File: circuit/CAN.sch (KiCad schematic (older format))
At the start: 4 parts

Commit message: 変更点忘れた
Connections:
- net +5V: no longer U?.3 (VDD)
- net TxD: now reaches U?.1 (TXD)
- net RxD: now reaches U?.4 (RXD)
- new net +3V3: U?.3 (VDD)
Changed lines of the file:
@@
 LIBS:robocon_sch
 LIBS:YASU
+LIBS:stm32
 LIBS:ServoDriver-cache
 EELAYER 25 0
@@
 $EndComp
 Wire Wire Line
-	3300 1900 3200 1900
+	3200 1900 3300 1900
 Wire Wire Line
 	3400 1900 3500 1900
@@
 	4600 1900 4700 1900
 Wire Wire Line
-	3700 1900 3600 1900
+	3600 1900 3700 1900
 Wire Wire Line
 	3650 1900 3650 2000
@@
 	1    0    0    -1
 $EndComp
-$Comp
-L +5V #PWR?
-U 1 1 594C7987
+Wire Wire Line
+	2250 1850 2250 1950
+$Comp
+L +3.3V #PWR?
+U 1 1 594E28CB
 P 2250 1850
 F 0 "#PWR?" H 2250 1700 50  0001 C CNN
-F 1 "+5V" H 2250 1990 50  0000 C CNN
+F 1 "+3.3V" H 2250 1990 50  0000 C CNN
 F 2 "" H 2250 1850 50  0001 C CNN
 F 3 "" H 2250 1850 50  0001 C CNN
@@
 $EndComp
 Wire Wire Line
-	2250 1850 2250 1950
+	1750 2250 1650 2250
+Wire Wire Line
+	1650 2150 1750 2150
+Text HLabel 1650 2250 0    60   Input ~ 0
+RxD
+Text HLabel 1650 2150 0    60   Output ~ 0
+TxD
 $EndSCHEMATC

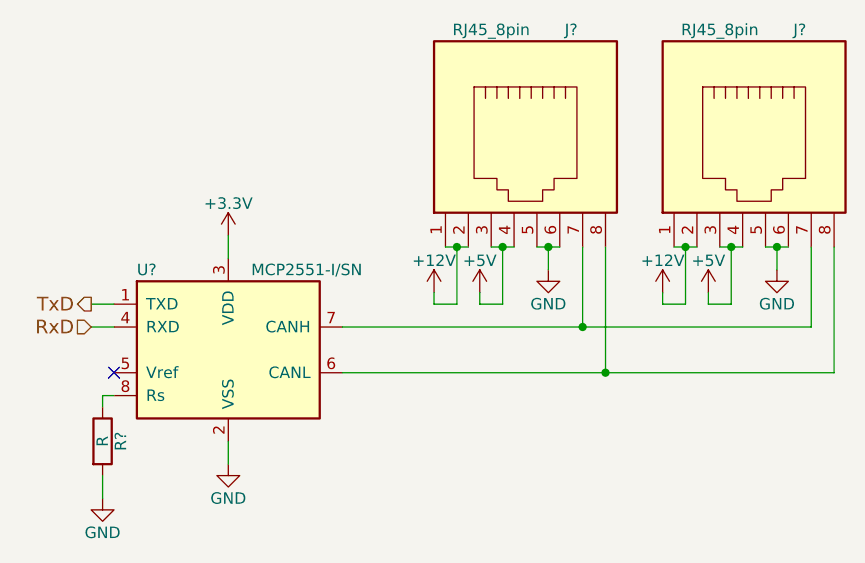
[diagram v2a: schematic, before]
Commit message: Servoのchを4->6に変更
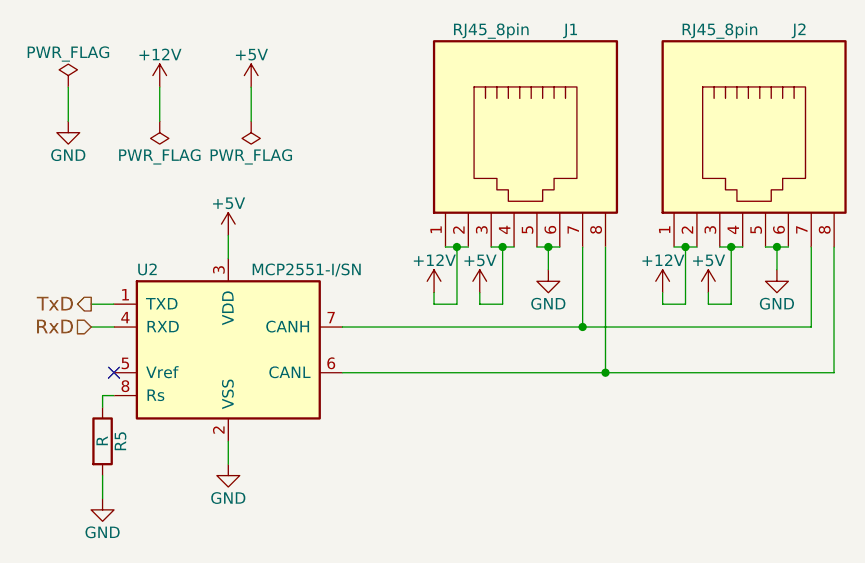
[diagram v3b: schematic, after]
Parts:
- J1, J2: renamed from J?; footprint (none) -> robocon_pcb:7810-8P8C
- gave numbers to parts that had none: 2
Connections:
- net +3V3 is gone; now on net +5V: U2.3 (VDD)
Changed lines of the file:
@@
 LIBS:contrib
 LIBS:valves
+LIBS:stm32
 LIBS:robocon_sch
+LIBS:SamacSys_Parts
 LIBS:YASU
-LIBS:stm32
 LIBS:ServoDriver-cache
 EELAYER 25 0
@@
 $Descr A4 11693 8268
 encoding utf-8
-Sheet 5 6
+Sheet 3 6
 Title ""
 Date ""
@@
 $EndDescr
 $Comp
-L RJ45_8pin J?
+L RJ45_8pin J1
 U 1 1 594B77B8
 P 3550 1450
-F 0 "J?" H 3750 1950 50  0000 C CNN
+F 0 "J1" H 3750 1950 50  0000 C CNN
 F 1 "RJ45_8pin" H 3400 1950 50  0000 C CNN
-F 2 "" H 3550 1450 50  0001 C CNN
+F 2 "robocon_pcb:7810-8P8C" H 3550 1450 50  0001 C CNN
 F 3 "" H 3550 1450 50  0001 C CNN
 	1    3550 1450
@@
 $EndComp
 $Comp
-L RJ45_8pin J?
+L RJ45_8pin J2
 U 1 1 594B7814
 P 4550 1450
-F 0 "J?" H 4750 1950 50  0000 C CNN
+F 0 "J2" H 4750 1950 50  0000 C CNN
 F 1 "RJ45_8pin" H 4400 1950 50  0000 C CNN
-F 2 "" H 4550 1450 50  0001 C CNN
+F 2 "robocon_pcb:7810-8P8C" H 4550 1450 50  0001 C CNN
 F 3 "" H 4550 1450 50  0001 C CNN
 	1    4550 1450
@@
 Connection ~ 3450 1900
 $Comp
-L +5V #PWR?
+L +5V #PWR015
 U 1 1 594C7289
 P 3350 2100
-F 0 "#PWR?" H 3350 1950 50  0001 C CNN
+F 0 "#PWR015" H 3350 1950 50  0001 C CNN
 F 1 "+5V" H 3350 2240 50  0000 C CNN
 F 2 "" H 3350 2100 50  0001 C CNN
@@
 Connection ~ 3250 1900
 $Comp
-L +12V #PWR?
+L +12V #PWR016
 U 1 1 594C7323
 P 3150 2100
-F 0 "#PWR?" H 3150 1950 50  0001 C CNN
+F 0 "#PWR016" H 3150 1950 50  0001 C CNN
 F 1 "+12V" H 3150 2240 50  0000 C CNN
 F 2 "" H 3150 2100 50  0001 C CNN
@@
 $EndComp
 $Comp
-L GND #PWR?
+L GND #PWR017
 U 1 1 594C734F
 P 3650 2000
-F 0 "#PWR?" H 3650 1750 50  0001 C CNN
+F 0 "#PWR017" H 3650 1750 50  0001 C CNN
 F 1 "GND" H 3650 1850 50  0000 C CNN
 F 2 "" H 3650 2000 50  0001 C CNN
@@
 	4450 1900 4450 2150
 $Comp
-L +5V #PWR?
+L +5V #PWR018
 U 1 1 594C746C
 P 4350 2100
-F 0 "#PWR?" H 4350 1950 50  0001 C CNN
+F 0 "#PWR018" H 4350 1950 50  0001 C CNN
 F 1 "+5V" H 4350 2240 50  0000 C CNN
 F 2 "" H 4350 2100 50  0001 C CNN
@@
 	4150 2150 4150 2100
 $Comp
-L +12V #PWR?
+L +12V #PWR019
 U 1 1 594C7477
 P 4150 2100
-F 0 "#PWR?" H 4150 1950 50  0001 C CNN
+F 0 "#PWR019" H 4150 1950 50  0001 C CNN
 F 1 "+12V" H 4150 2240 50  0000 C CNN
 F 2 "" H 4150 2100 50  0001 C CNN
@@
 $EndComp
 $Comp
-L GND #PWR?
+L GND #PWR020
 U 1 1 594C747D
 P 4650 2000
-F 0 "#PWR?" H 4650 1750 50  0001 C CNN
+F 0 "#PWR020" H 4650 1750 50  0001 C CNN
 F 1 "GND" H 4650 1850 50  0000 C CNN
 F 2 "" H 4650 2000 50  0001 C CNN
@@
 Connection ~ 4650 1900
 $Comp
-L MCP2551-I/SN U?
+L MCP2551-I/SN U2
 U 1 1 594C7542
 P 2250 2350
-F 0 "U?" H 1850 2700 50  0000 L CNN
+F 0 "U2" H 1850 2700 50  0000 L CNN
 F 1 "MCP2551-I/SN" H 2350 2700 50  0000 L CNN
 F 2 "Housings_SOIC:SOIC-8_3.9x4.9mm_Pitch1.27mm" H 2250 1850 50  0001 C CIN
@@
 Connection ~ 3900 2450
 $Comp
-L GND #PWR?
+L GND #PWR021
 U 1 1 594C775E
 P 2250 2850
-F 0 "#PWR?" H 2250 2600 50  0001 C CNN
+F 0 "#PWR021" H 2250 2600 50  0001 C CNN
 F 1 "GND" H 2250 2700 50  0000 C CNN
 F 2 "" H 2250 2850 50  0001 C CNN
@@
 $EndComp
 $Comp
-L R R?
+L R R5
 U 1 1 594C777D
 P 1700 2750
-F 0 "R?" V 1780 2750 50  0000 C CNN
+F 0 "R5" V 1780 2750 50  0000 C CNN
 F 1 "R" V 1700 2750 50  0000 C CNN
 F 2 "" V 1630 2750 50  0001 C CNN
@@
 	2250 2850 2250 2750
 $Comp
-L GND #PWR?
+L GND #PWR022
 U 1 1 594C7944
 P 1700 3000
-F 0 "#PWR?" H 1700 2750 50  0001 C CNN
+F 0 "#PWR022" H 1700 2750 50  0001 C CNN
 F 1 "GND" H 1700 2850 50  0000 C CNN
 F 2 "" H 1700 3000 50  0001 C CNN
@@
 Wire Wire Line
 	2250 1850 2250 1950
-$Comp
-L +3.3V #PWR?
-U 1 1 594E28CB
-P 2250 1850
-F 0 "#PWR?" H 2250 1700 50  0001 C CNN
-F 1 "+3.3V" H 2250 1990 50  0000 C CNN
-F 2 "" H 2250 1850 50  0001 C CNN
-F 3 "" H 2250 1850 50  0001 C CNN
-	1    2250 1850
-	1    0    0    -1
-$EndComp
 Wire Wire Line
 	1750 2250 1650 2250
@@
 Text HLabel 1650 2150 0    60   Output ~ 0
 TxD
+$Comp
+L +5V #PWR023
+U 1 1 59730CDC
+P 2250 1850
+F 0 "#PWR023" H 2250 1700 50  0001 C CNN
+F 1 "+5V" H 2250 1990 50  0000 C CNN
+F 2 "" H 2250 1850 50  0001 C CNN
+F 3 "" H 2250 1850 50  0001 C CNN
+	1    2250 1850
+	1    0    0    -1
+$EndComp
+$Comp
+L PWR_FLAG #FLG024
+U 1 1 5973705E
+P 1950 1350
+F 0 "#FLG024" H 1950 1425 50  0001 C CNN
+F 1 "PWR_FLAG" H 1950 1500 50  0000 C CNN
+F 2 "" H 1950 1350 50  0001 C CNN
+F 3 "" H 1950 1350 50  0001 C CNN
+	1    1950 1350
+	-1   0    0    1
+$EndComp
+$Comp
+L +12V #PWR025
+U 1 1 59737180
+P 1950 1200
+F 0 "#PWR025" H 1950 1050 50  0001 C CNN
+F 1 "+12V" H 1950 1340 50  0000 C CNN
+F 2 "" H 1950 1200 50  0001 C CNN
+F 3 "" H 1950 1200 50  0001 C CNN
+	1    1950 1200
+	1    0    0    -1
+$EndComp
+$Comp
+L +5V #PWR026
+U 1 1 597371B7
+P 2350 1200
+F 0 "#PWR026" H 2350 1050 50  0001 C CNN
+F 1 "+5V" H 2350 1340 50  0000 C CNN
+F 2 "" H 2350 1200 50  0001 C CNN
+F 3 "" H 2350 1200 50  0001 C CNN
+	1    2350 1200
+	1    0    0    -1
+$EndComp
+Wire Wire Line
+	1950 1200 1950 1350
+$Comp
+L PWR_FLAG #FLG027
+U 1 1 597371FE
+P 2350 1350
+F 0 "#FLG027" H 2350 1425 50  0001 C CNN
+F 1 "PWR_FLAG" H 2350 1500 50  0000 C CNN
+F 2 "" H 2350 1350 50  0001 C CNN
+F 3 "" H 2350 1350 50  0001 C CNN
+	1    2350 1350
+	-1   0    0    1
+$EndComp
+Wire Wire Line
+	2350 1350 2350 1200
+$Comp
+L PWR_FLAG #FLG028
+U 1 1 59738D0E
+P 1550 1200
+F 0 "#FLG028" H 1550 1275 50  0001 C CNN
+F 1 "PWR_FLAG" H 1550 1350 50  0000 C CNN
+F 2 "" H 1550 1200 50  0001 C CNN
+F 3 "" H 1550 1200 50  0001 C CNN
+	1    1550 1200
+	1    0    0    -1
+$EndComp
+Wire Wire Line
+	1550 1200 1550 1350
+$Comp
+L GND #PWR029
+U 1 1 59738E38
+P 1550 1350
+F 0 "#PWR029" H 1550 1100 50  0001 C CNN
+F 1 "GND" H 1550 1200 50  0000 C CNN
+F 2 "" H 1550 1350 50  0001 C CNN
+F 3 "" H 1550 1350 50  0001 C CNN
+	1    1550 1350
+	1    0    0    -1
+$EndComp
 $EndSCHEMATC

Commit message: 回路図と部品表完了
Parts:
- R5: footprint (none) -> Resistors_SMD:R_0603_HandSoldering
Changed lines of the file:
@@
 F 0 "R5" V 1780 2750 50  0000 C CNN
 F 1 "R" V 1700 2750 50  0000 C CNN
-F 2 "" V 1630 2750 50  0001 C CNN
+F 2 "Resistors_SMD:R_0603_HandSoldering" V 1630 2750 50  0001 C CNN
 F 3 "" H 1700 2750 50  0001 C CNN
 	1    1700 2750

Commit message: 配線完了
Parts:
- U2: footprint Housings_SOIC:SOIC-8_3.9x4.9mm_Pitch1.27mm -> Housings_DIP:DIP-8_W7.62mm_Socket_LongPads
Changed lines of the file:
@@
 F 0 "U2" H 1850 2700 50  0000 L CNN
 F 1 "MCP2551-I/SN" H 2350 2700 50  0000 L CNN
-F 2 "Housings_SOIC:SOIC-8_3.9x4.9mm_Pitch1.27mm" H 2250 1850 50  0001 C CIN
+F 2 "Housings_DIP:DIP-8_W7.62mm_Socket_LongPads" H 2250 1850 50  0001 C CIN
 F 3 "" H 2250 2350 50  0001 C CNN
 	1    2250 2350

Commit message: チップ抵抗の大きさ変更とガーバー出力のための手直し
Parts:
- R5: footprint Resistors_SMD:R_0603_HandSoldering -> YASU:R_0603_HandSoldering_LP
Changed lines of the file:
@@
 F 0 "R5" V 1780 2750 50  0000 C CNN
 F 1 "R" V 1700 2750 50  0000 C CNN
-F 2 "Resistors_SMD:R_0603_HandSoldering" V 1630 2750 50  0001 C CNN
+F 2 "YASU:R_0603_HandSoldering_LP" V 1630 2750 50  0001 C CNN
 F 3 "" H 1700 2750 50  0001 C CNN
 	1    1700 2750
